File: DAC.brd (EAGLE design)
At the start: 81.3 x 76.2 mm, 87 parts, among them IC1 LM2662, IC2 PCM1793, IC3 OPA2134PA, IC4 LMH6643, J1 USBSMD, J2 RCJ-21XXMILL, U1 LDO-TPS78233, U2 PCM2707, Y1 12MHz/20pF

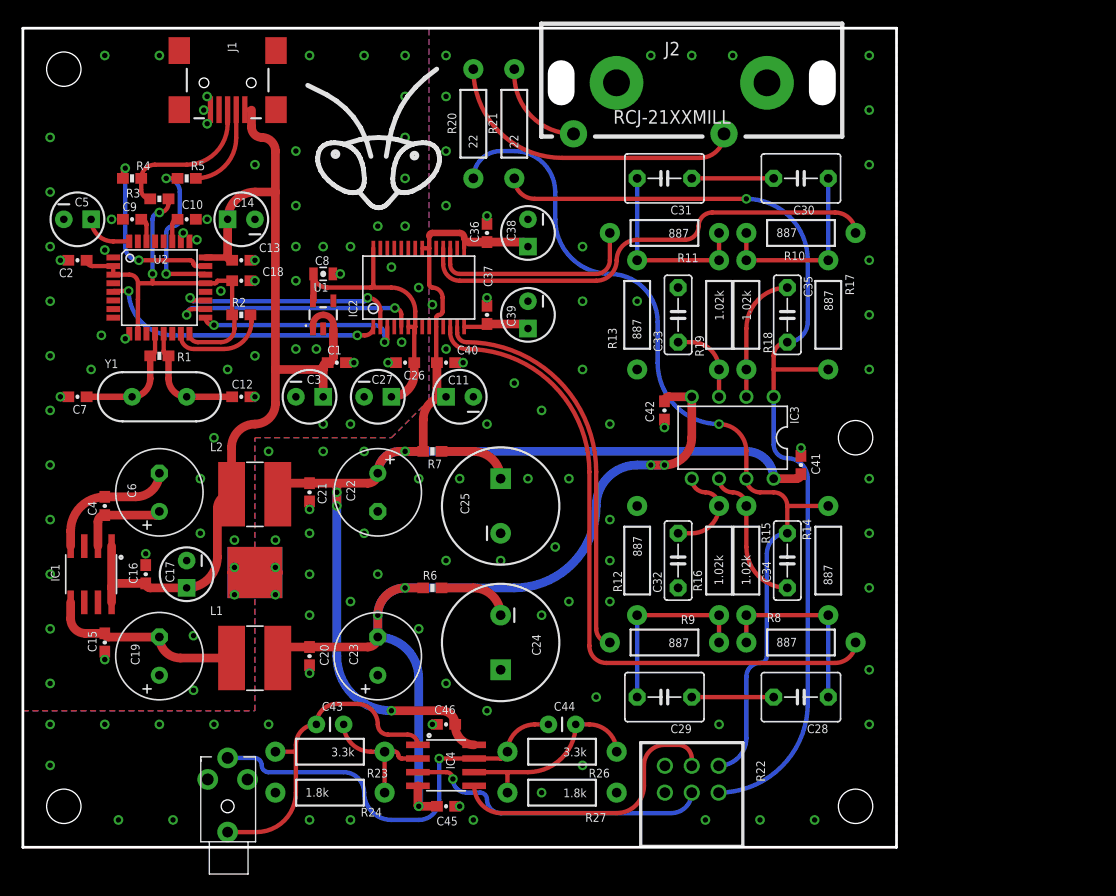
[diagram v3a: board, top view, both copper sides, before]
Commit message: Bias correction
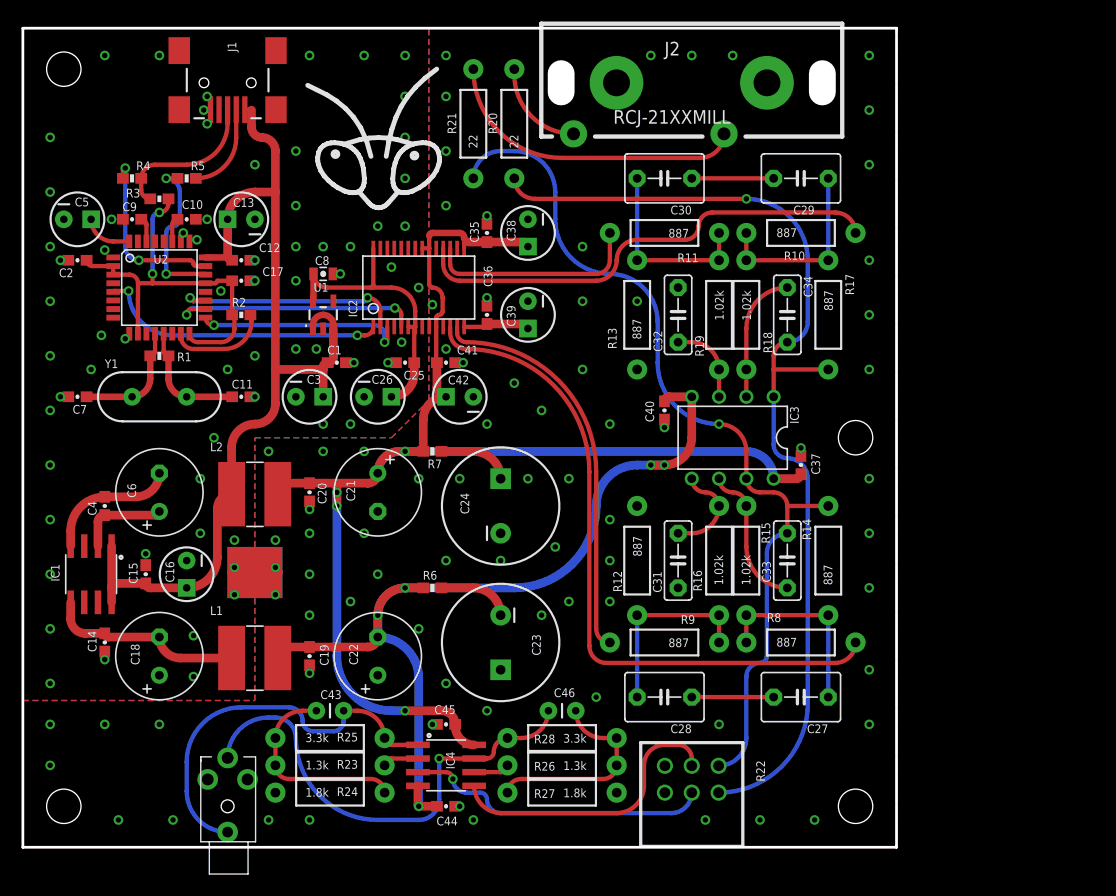
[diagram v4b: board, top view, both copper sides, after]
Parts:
- added R25, R28: 3.3k, SparkFun-Resistors:AXIAL-0.4
- C11: value 10uF -> 20pF; device SparkFun-Capacitors:CPOL-RADIAL-10UF-25V -> SparkFun-Capacitors:0603-CAP
- C12: value 20pF -> 0.1uF
- C13, C16, C26: value 0.1uF -> 10uF; device SparkFun-Capacitors:0603-CAP -> SparkFun-Capacitors:CPOL-RADIAL-10UF-25V
- C14, C17: value 10uF -> 1.0uF; device SparkFun-Capacitors:CPOL-RADIAL-10UF-25V -> SparkFun-Capacitors:0603-CAP
- C15, C41: value 1.0uF -> 0.1uF
- C18: value 1.0uF -> 220uF/Low ESR; device SparkFun-Capacitors:0603-CAP -> rcl:E3,5-8
- C19: value 220uF/Low ESR -> 1.0uF; device rcl:E3,5-8 -> SparkFun-Capacitors:0603-CAP
- C21: value 1.0uF -> 220uF; device SparkFun-Capacitors:0603-CAP -> rcl:E3,5-8
- C23: value 220uF -> 1000uF; device rcl:E3,5-8 -> SparkFun-Capacitors:CPOL-RADIAL-1000UF-25V
- C25: value 1000uF -> 0.1uF; device SparkFun-Capacitors:CPOL-RADIAL-1000UF-25V -> SparkFun-Capacitors:0603-CAP
- C27: value 10uF -> 4.7nF; device SparkFun-Capacitors:CPOL-RADIAL-10UF-25V -> capacitor-wima:C5B4.5
- C31: value 4.7nF -> 1nF; device capacitor-wima:C5B4.5 -> capacitor-wima:C5B2.5
- C35: value 1nF -> 0.1uF; device capacitor-wima:C5B2.5 -> SparkFun-Capacitors:0603-CAP
- C37, C40: value 0.1uF -> 1.0uF
- C42: value 1.0uF -> 10uF; device SparkFun-Capacitors:0603-CAP -> SparkFun-Capacitors:CPOL-RADIAL-10UF-25V
- C44: value 100pF -> 1.0uF; device SparkFun-Capacitors:CAP-PTH-SMALL -> SparkFun-Capacitors:0603-CAP
- C46: value 1.0uF -> 100pF; device SparkFun-Capacitors:0603-CAP -> SparkFun-Capacitors:CAP-PTH-SMALL
- R23, R26: value 3.3k -> 1.3k
- moved C29 49.9 mm to (72.4, 62.2)
- moved C27 48.3 mm to (72.4, 14.0), turned to 180 degrees
- moved C14 41.4 mm to (7.62, 19.1), turned to 90 degrees
- moved C18 35.7 mm to (12.7, 17.8), turned to 90 degrees
- moved C31 35.6 mm to (61.0, 26.7), turned to 90 degrees
- moved C41 34.4 mm to (39.4, 45.1), turned to 0 degrees
- moved C37 32.4 mm to (72.4, 35.6)
- moved C35 29.0 mm to (43.2, 57.1), turned to 90 degrees
- moved C17 27.8 mm to (20.3, 52.7), turned to 0 degrees
- moved C33 25.0 mm to (71.1, 26.7), turned to 90 degrees
- moved C32 22.9 mm to (61.0, 49.5), turned to 270 degrees
- moved C34 22.9 mm to (71.1, 49.5), turned to 270 degrees
- moved C40 20.8 mm to (59.7, 40.6), turned to 270 degrees
- moved C11 20.3 mm to (20.3, 41.9), turned to 0 degrees
- moved C42 19.1 mm to (40.6, 41.9), turned to 180 degrees
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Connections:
- new net N$6: IC4.6, R26.P$2
- new net N$7: IC4.2, R23.P$2
- net +5V: now also C20.1, C21.+, C35.1, C37.1, C42.1, C45.1; no longer C11.1, C21.1, C22.+, C36.1, C40.1, C46.1
- net -5V: now also C19.2, C22.-, C40.1, C44.1; no longer C20.2, C23.-, C42.1, C45.1
- net 3V3: now also C25.1; no longer C27.1
- net AGND: now also C19.1, C20.2, C21.-, C22.+, C24.-, C31.1, C35.2, C44.2; no longer C11.2, C20.1, C21.2, C22.-, C24.+, C25.-, C33.1, C46.2
- net GND: now also C11.2, C14.1, C15.2, C18.+, C25.2; no longer C14.2, C15.1, C18.2, C19.+, C27.2
- net HP_L: now also R25.P$2; no longer R23.P$2
- net HP_R: now also C46.1, R28.P$2; no longer C44.1, R26.P$2
- net INT3V3: now also C17.1; no longer C18.1
- net N$10: now also C23.-; no longer C24.-
- net N$14: now also R25.P$1; no longer IC4.2
- net N$16: now also C29.2, C30.1; no longer C30.2, C31.1
- net N$17: now also C30.2; no longer C31.2
- net N$18: now also C29.1; no longer C30.1
- net N$19: now also C46.2, R28.P$1; no longer C44.2, IC4.6
- net N$20: now also C28.2; no longer C29.2
- net N$21: now also C27.1; no longer C28.1
- net N$22: now also C27.2, C28.1; no longer C28.2, C29.1
- net N$5: now also C36.1; no longer C37.1
- net N$8: now also C24.+; no longer C25.+
- net N$9: now also C14.2, C18.-; no longer C15.2, C19.-
- net OPL+: now also C32.2; no longer C33.2
- net OPL-: now also C34.1; no longer C35.1
- net OPR+: now also C31.2; no longer C32.2
- net OPR-: now also C33.1; no longer C34.1
- net OUT_L: now also R20.P$2; no longer R21.P$2
- net OUT_L*: now also C34.2, R20.P$1; no longer C35.2, R21.P$1
- net OUT_R: now also R21.P$2; no longer R20.P$2
- net OUT_R*: now also C33.2, R21.P$1; no longer C34.2, R20.P$1
- net VCC: now also C12.1, C15.1; no longer C14.1, C17.1
- net XTO: now also C11.1; no longer C12.1
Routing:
- net N$14: track 12.0 -> 18.6 mm
- net HP_L: track 28.7 -> 35.3 mm
- net HP_R: track 38.1 -> 41.8 mm
- net N$6: track 0.00 -> 3.36 mm
- net N$7: track 0.00 -> 3.36 mm
- net N$19: track 18.1 -> 18.6 mm
